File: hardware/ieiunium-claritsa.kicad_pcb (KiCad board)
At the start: 2 copper layers, 35 parts, among them SW1 SWITCH

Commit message: Proceed PCB
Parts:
- C1: footprint Capacitors:CAP_0805 -> Capacitors:CAP_0603
- moved C4 103.2 mm to (208.0, 49.0), turned to 180 degrees
- moved C3 97.1 mm to (206.5, 62.0)
- moved C7 95.8 mm to (197.5, 50.0), turned to 90 degrees
- moved C1 88.2 mm to (201.5, 62.0), turned to 180 degrees
- moved C6 75.8 mm to (205.0, 49.0)
- moved F1 75.6 mm to (210.0, 53.0), turned to 180 degrees
- moved R2 75.6 mm to (201.5, 63.5)
- moved C2 75.4 mm to (198.0, 63.0), turned to 90 degrees
- moved C8 74.3 mm to (196.5, 56.0), turned to 270 degrees
- moved TP9 72.6 mm to (181.0, 59.0)
- moved R5 71.4 mm to (206.5, 66.5), turned to 180 degrees
- moved R3 69.2 mm to (206.5, 63.5), turned to 180 degrees
- moved D1 68.4 mm to (198.5, 66.5)
- moved D2 68.2 mm to (195.0, 55.5), turned to 270 degrees
- moved XL2 65.2 mm to (176.0, 50.0)
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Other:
- net class Default: via_dia 0.6 -> 0.8
- net class PWR added: clearance 0.3, trace_width 0.5, via_dia 0.8, via_drill 0.4

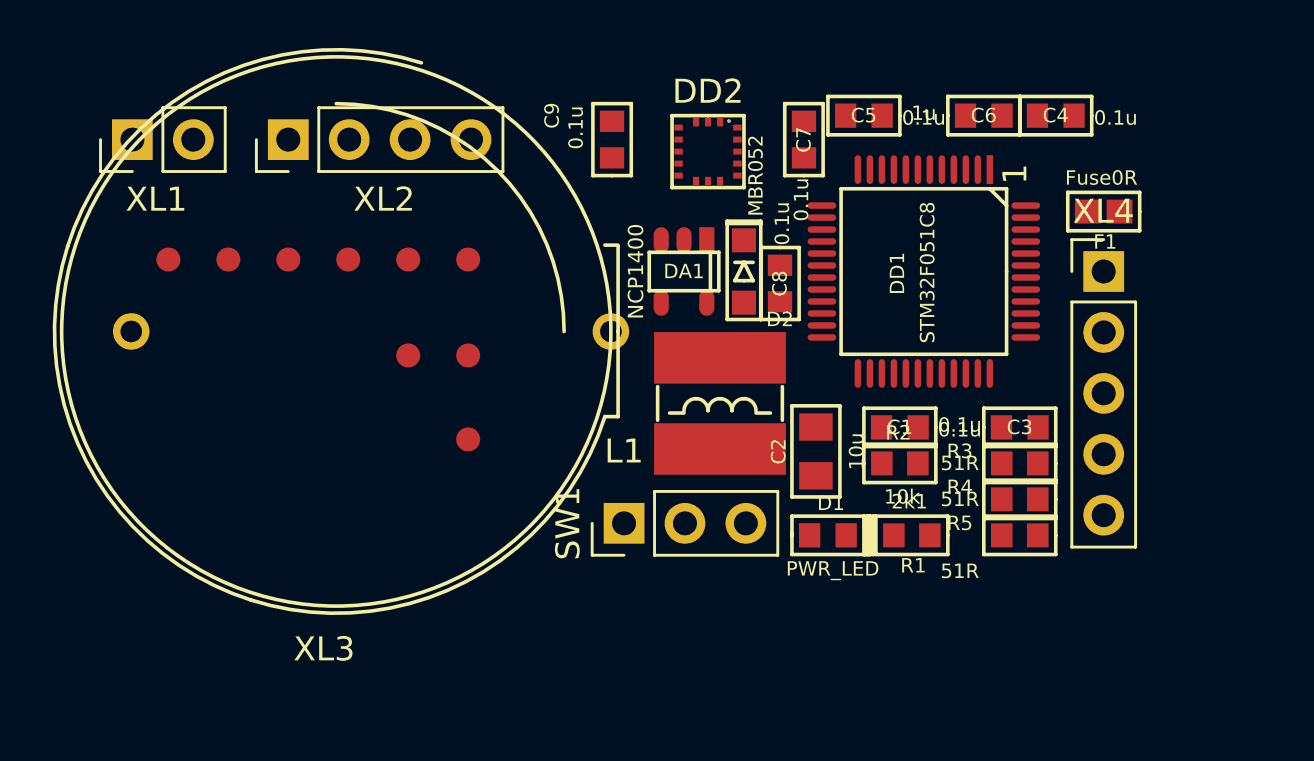
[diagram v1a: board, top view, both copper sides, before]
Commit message: Increase PCB size
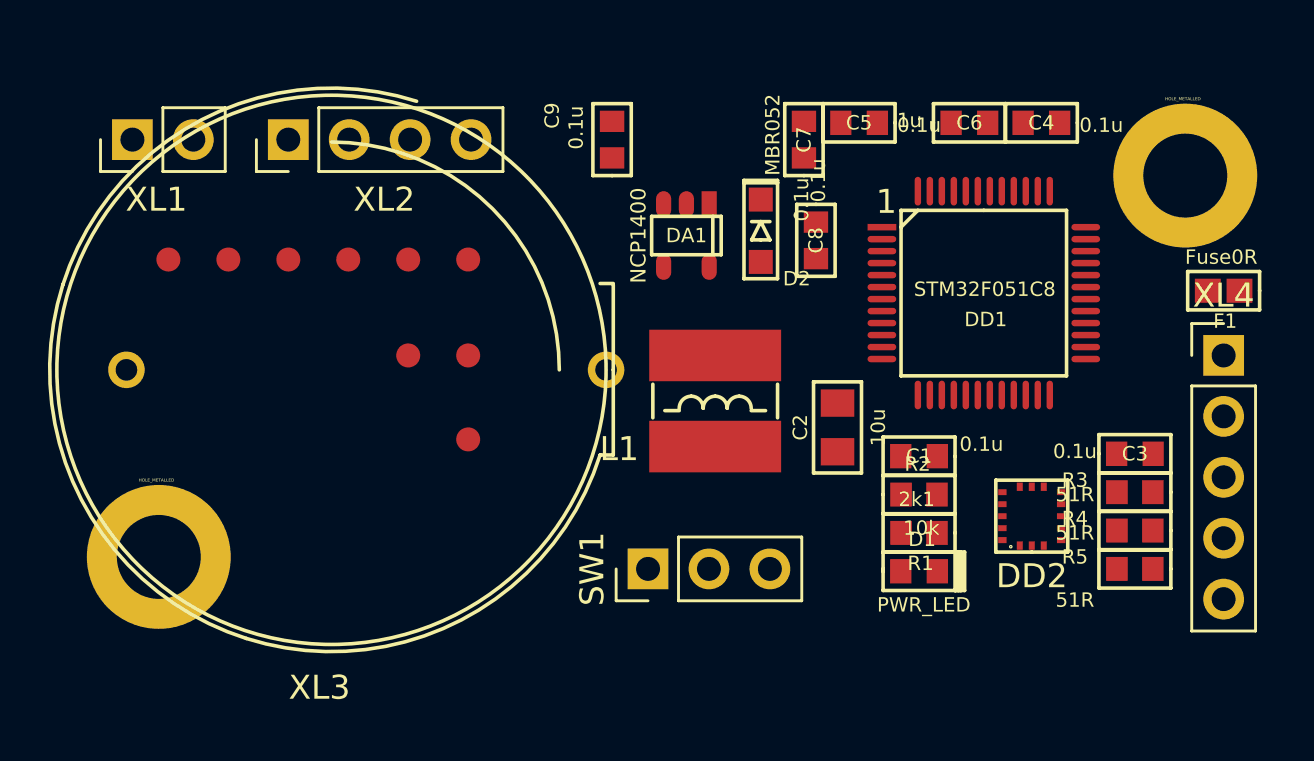
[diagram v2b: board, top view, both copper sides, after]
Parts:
- added HOLE1: HOLE_METALLED, PCB:Hole3_5_out6mm, F.Cu at (170.6, 67.4)
- added HOLE2: HOLE_METALLED, PCB:Hole3_5_out6mm, F.Cu at (213.4, 51.5)
- moved DD2 20.3 mm to (207.0, 65.7), turned to 180 degrees
- moved XL4 6.10 mm to (215.0, 59.0)
- moved F1 5.99 mm to (215.0, 56.3)
- moved R5 5.00 mm to (211.3, 67.9)
- moved R4 4.97 mm to (211.3, 66.3)
- moved R3 4.95 mm to (211.3, 64.7)
- moved C3 4.92 mm to (211.3, 63.1)
- moved D1 4.09 mm to (202.3, 68.0)
- moved DD1 2.66 mm to (205.0, 56.4), turned to 0 degrees
- moved C8 2.34 mm to (198.0, 54.2)
- moved SW1 2.15 mm to (191.0, 67.9)
- moved D2 1.84 mm to (195.7, 53.8)
- moved XL3 1.61 mm to (177.8, 59.6)
- moved R2 1.53 mm to (202.3, 64.8)
- moved DA1 1.50 mm to (192.6, 54.0)
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
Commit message: PCB start
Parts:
- XL3: footprint Installation:BH-6_CR2032 -> BH-6_CR2032
- moved C1 1.84 mm to (200.5, 62.8), turned to 90 degrees
- moved DD2 1.30 mm to (205.7, 65.7)
- moved R2 1.14 mm to (201.2, 65.1), turned to 180 degrees
- moved D1 1.12 mm to (201.2, 68.2)
- moved R1 1.12 mm to (201.2, 66.6)
- moved L1 0.85 mm to (194.6, 61.2)
- moved C8 0.51 mm to (197.5, 54.3)
- moved C2 0.45 mm to (198.7, 62.4)
- moved D2 0.20 mm to (195.5, 53.8)
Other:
- board outline added: 50 x 23 mm
